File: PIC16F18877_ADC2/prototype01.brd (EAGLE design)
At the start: 72 x 47 mm, 18 parts, among them CN1 PIC_CN_H, CN2 12V_IN, CN3 ADC_IN, SW1 10-XX, U1 XC6202P502TB, U2 PIC16F18877-I/P, X1 20MHz

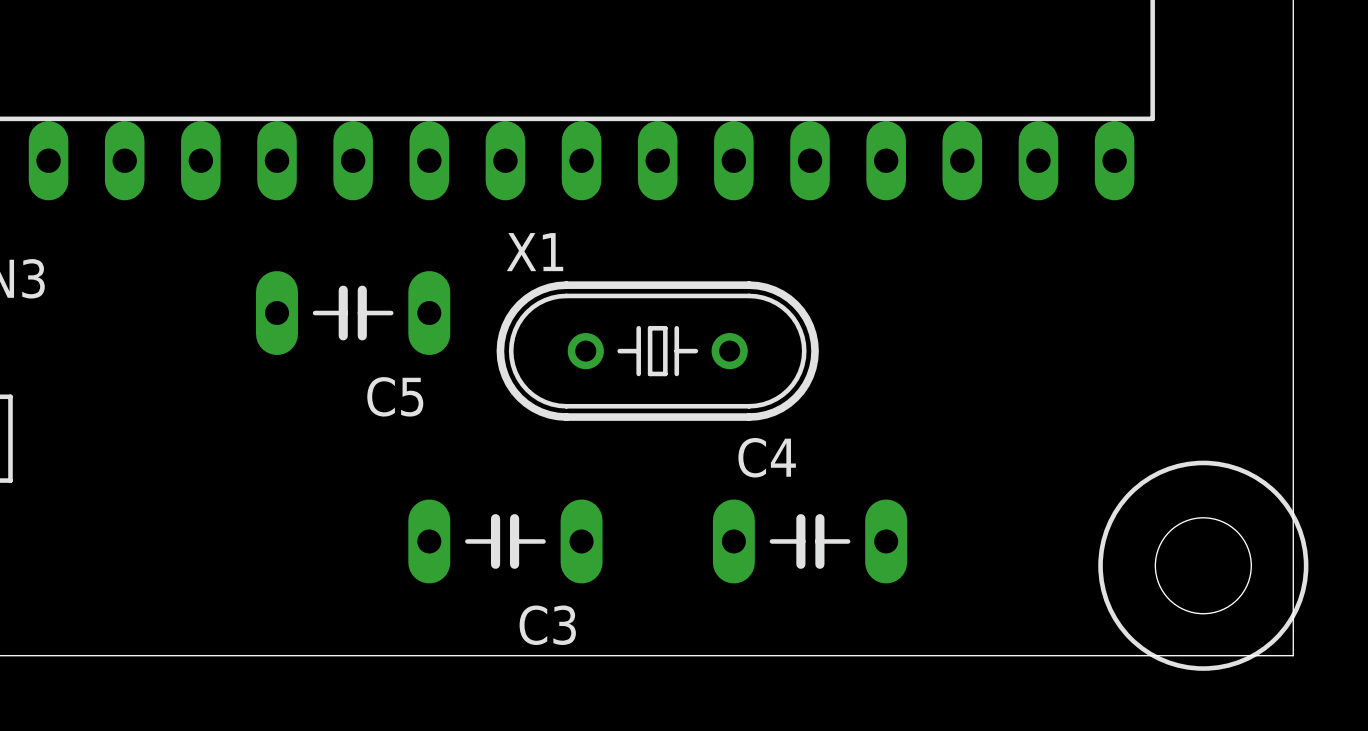
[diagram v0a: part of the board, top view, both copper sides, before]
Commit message: 回路図を修正
LCDモジュール(AE-AQM1602A)を回路に追加
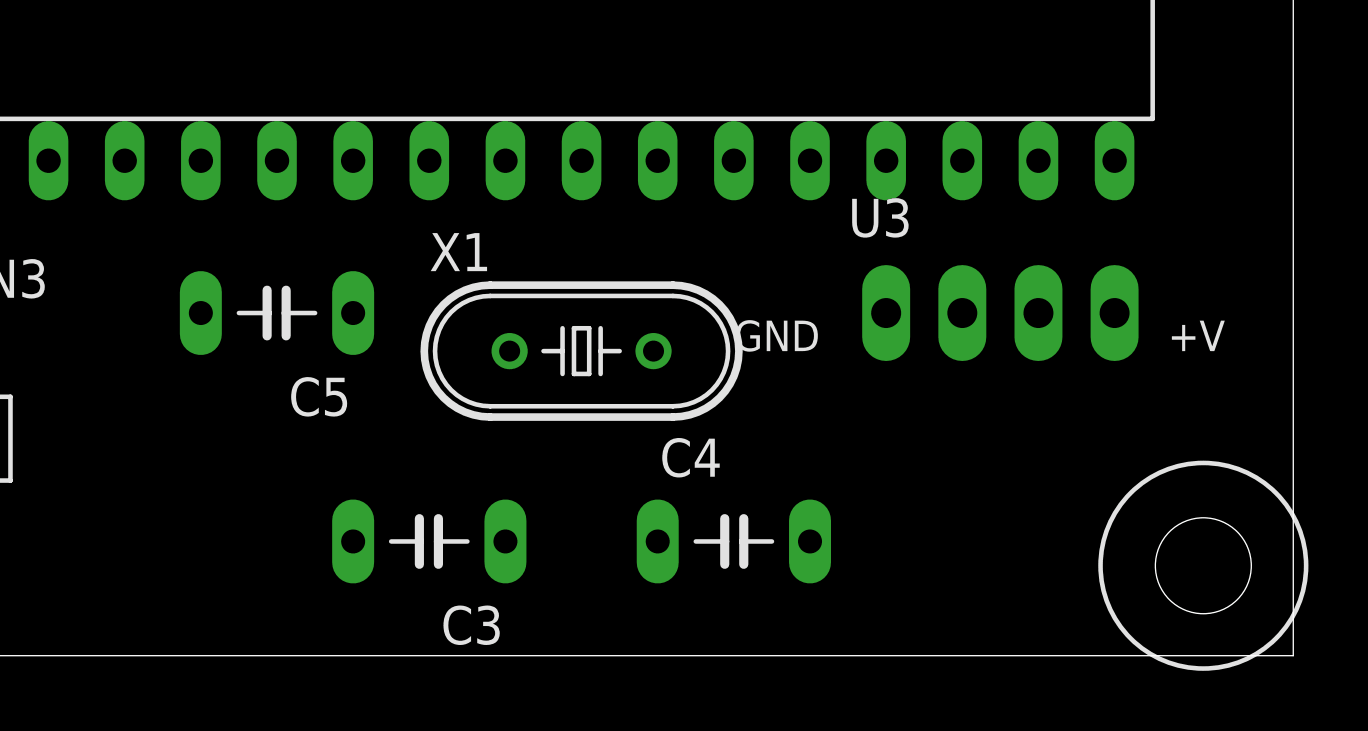
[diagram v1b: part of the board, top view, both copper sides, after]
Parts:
- added U3: AE-AQM1602A, PartsForProto:AE-AQM1602A
- moved C3 2.54 mm to (43.2, 3.81)
- moved C4 2.54 mm to (53.3, 3.81)
- moved C5 2.54 mm to (38.1, 11.4)
- moved X1 2.54 mm to (48.3, 10.2)
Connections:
- new net N$1: U2.18, U3.3
- new net N$5: U2.23, U3.2
- net +5V: now also U3.4
- net 0V: now also U3.1
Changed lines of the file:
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@@
 <element name="C1" library="Parts" package="CAP_200MIL" value="1uF" x="13.97" y="38.1" rot="R270"/>
 <element name="C2" library="Parts" package="CAP_200MIL" value="1uF" x="26.67" y="38.1" rot="R270"/>
-<element name="C3" library="Parts" package="CAP_200MIL" value="22pF" x="45.72" y="3.81" rot="R180"/>
-<element name="C4" library="Parts" package="CAP_200MIL" value="22pF" x="55.88" y="3.81"/>
-<element name="C5" library="Parts" package="CAP_200MIL" value="0.1uF" x="40.64" y="11.43" rot="R180"/>
+<element name="C3" library="Parts" package="CAP_200MIL" value="22pF" x="43.18" y="3.81" rot="R180"/>
+<element name="C4" library="Parts" package="CAP_200MIL" value="22pF" x="53.34" y="3.81"/>
+<element name="C5" library="Parts" package="CAP_200MIL" value="0.1uF" x="38.1" y="11.43" rot="R180"/>
 <element name="C6" library="Parts" package="CAP_200MIL" value="0.1uF" x="35.56" y="36.83" rot="R180"/>
 <element name="CN1" library="Connectors" package="HEADER_6PIN" value="PIC_CN_H" x="7.62" y="25.4" rot="R90"/>
@@
 <element name="U1" library="Parts" package="TO92-LINE" value="XC6202P502TB" x="17.78" y="40.64"/>
 <element name="U2" library="Parts" package="DIL40" value="PIC16F18877-I/P" x="41.91" y="24.13"/>
-<element name="X1" library="Parts" package="HC-49/S" value="20MHz" x="50.8" y="10.16"/>
+<element name="X1" library="Parts" package="HC-49/S" value="20MHz" x="48.26" y="10.16"/>
 <element name="H1" library="Generic" package="3,2" value="MOUNT_HOLE_3.2" x="3" y="44"/>
 <element name="H2" library="Generic" package="3,2" value="MOUNT_HOLE_3.2" x="3" y="3"/>
@@
 <element name="H4" library="Generic" package="3,2" value="MOUNT_HOLE_3.2" x="69" y="44"/>
 <element name="CN2" library="Connectors" package="HEADER_L_2PIN" value="12V_IN" x="19.05" y="8.89" rot="R180"/>
+<element name="U3" library="PartsForProto" package="AE-AQM1602A" value="AE-AQM1602A" x="58.42" y="11.43"/>
 </elements>
 <signals>
@@
 <contactref element="CN3" pad="2"/>
 <contactref element="CN2" pad="2"/>
-<wire x1="40.64" y1="31.75" x2="33.02" y2="36.83" width="0" layer="19" extent="1-1"/>
+<contactref element="U3" pad="1"/>
+<wire x1="33.02" y1="36.83" x2="40.64" y2="31.75" width="0" layer="19" extent="1-1"/>
 <wire x1="26.67" y1="35.56" x2="33.02" y2="36.83" width="0" layer="19" extent="1-1"/>
 <wire x1="20.32" y1="40.64" x2="26.67" y2="35.56" width="0" layer="19" extent="1-1"/>
@@
 <wire x1="3.81" y1="15.24" x2="7.62" y2="30.48" width="0" layer="19" extent="1-1"/>
 <wire x1="3.81" y1="10.16" x2="3.81" y2="15.24" width="0" layer="19" extent="1-1"/>
-<wire x1="20.32" y1="10.16" x2="3.81" y2="10.16" width="0" layer="19" extent="1-1"/>
 <wire x1="45.72" y1="16.51" x2="40.64" y2="31.75" width="0" layer="19" extent="1-1"/>
-<wire x1="38.1" y1="11.43" x2="45.72" y2="16.51" width="0" layer="19" extent="1-1"/>
-<wire x1="58.42" y1="3.81" x2="38.1" y2="11.43" width="0" layer="19" extent="1-1"/>
-<wire x1="43.18" y1="3.81" x2="38.1" y2="11.43" width="0" layer="19" extent="1-1"/>
-<wire x1="27.94" y1="10.16" x2="3.81" y2="10.16" width="0" layer="19" extent="1-1"/>
+<wire x1="35.56" y1="11.43" x2="45.72" y2="16.51" width="0" layer="19" extent="1-1"/>
+<wire x1="40.64" y1="3.81" x2="35.56" y2="11.43" width="0" layer="19" extent="1-1"/>
+<wire x1="27.94" y1="10.16" x2="35.56" y2="11.43" width="0" layer="19" extent="1-1"/>
+<wire x1="20.32" y1="10.16" x2="27.94" y2="10.16" width="0" layer="19" extent="1-1"/>
+<wire x1="55.88" y1="3.81" x2="40.64" y2="3.81" width="0" layer="19" extent="1-1"/>
+<wire x1="58.42" y1="11.43" x2="3.81" y2="10.16" width="0" layer="19" extent="1-1"/>
 </signal>
 <signal name="+5V">
@@
 <contactref element="U2" pad="32"/>
 <contactref element="CN1" pad="2"/>
-<wire x1="7.62" y1="27.94" x2="11.43" y2="20.32" width="0" layer="19" extent="1-1"/>
-<wire x1="43.18" y1="11.43" x2="7.62" y2="27.94" width="0" layer="19" extent="1-1"/>
-<wire x1="38.1" y1="36.83" x2="43.18" y2="11.43" width="0" layer="19" extent="1-1"/>
+<contactref element="U3" pad="4"/>
+<wire x1="38.1" y1="31.75" x2="38.1" y2="36.83" width="0" layer="19" extent="1-1"/>
+<wire x1="43.18" y1="16.51" x2="38.1" y2="31.75" width="0" layer="19" extent="1-1"/>
+<wire x1="40.64" y1="11.43" x2="43.18" y2="16.51" width="0" layer="19" extent="1-1"/>
 <wire x1="17.78" y1="40.64" x2="38.1" y2="36.83" width="0" layer="19" extent="1-1"/>
 <wire x1="13.97" y1="40.64" x2="17.78" y2="40.64" width="0" layer="19" extent="1-1"/>
-<wire x1="38.1" y1="31.75" x2="17.78" y2="40.64" width="0" layer="19" extent="1-1"/>
-<wire x1="43.18" y1="16.51" x2="38.1" y2="31.75" width="0" layer="19" extent="1-1"/>
+<wire x1="7.62" y1="27.94" x2="13.97" y2="40.64" width="0" layer="19" extent="1-1"/>
+<wire x1="11.43" y1="20.32" x2="7.62" y2="27.94" width="0" layer="19" extent="1-1"/>
+<wire x1="66.04" y1="11.43" x2="11.43" y2="20.32" width="0" layer="19" extent="1-1"/>
 </signal>
 <signal name="OSC1">
@@
 <contactref element="C3" pad="1"/>
 <contactref element="U2" pad="13"/>
-<wire x1="48.4" y1="10.16" x2="48.26" y2="16.51" width="0" layer="19" extent="1-1"/>
-<wire x1="48.26" y1="3.81" x2="48.4" y2="10.16" width="0" layer="19" extent="1-1"/>
+<wire x1="45.86" y1="10.16" x2="48.26" y2="16.51" width="0" layer="19" extent="1-1"/>
+<wire x1="45.72" y1="3.81" x2="45.86" y2="10.16" width="0" layer="19" extent="1-1"/>
 </signal>
 <signal name="OSC2">
@@
 <contactref element="C4" pad="1"/>
 <contactref element="U2" pad="14"/>
-<wire x1="53.2" y1="10.16" x2="50.8" y2="16.51" width="0" layer="19" extent="1-1"/>
-<wire x1="53.34" y1="3.81" x2="53.2" y2="10.16" width="0" layer="19" extent="1-1"/>
+<wire x1="50.66" y1="10.16" x2="50.8" y2="16.51" width="0" layer="19" extent="1-1"/>
+<wire x1="50.8" y1="3.81" x2="50.66" y2="10.16" width="0" layer="19" extent="1-1"/>
 </signal>
 <signal name="N$3">
@@
 <wire x1="25.4" y1="10.16" x2="20.32" y2="16.51" width="0" layer="19" extent="1-1"/>
 </signal>
+<signal name="N$1">
+<contactref element="U3" pad="3"/>
+<contactref element="U2" pad="18"/>
+<wire x1="63.5" y1="11.43" x2="60.96" y2="16.51" width="0" layer="19" extent="1-1"/>
+</signal>
+<signal name="N$5">
+<contactref element="U3" pad="2"/>
+<contactref element="U2" pad="23"/>
+<wire x1="60.96" y1="11.43" x2="60.96" y2="31.75" width="0" layer="19" extent="1-1"/>
+</signal>
 </signals>

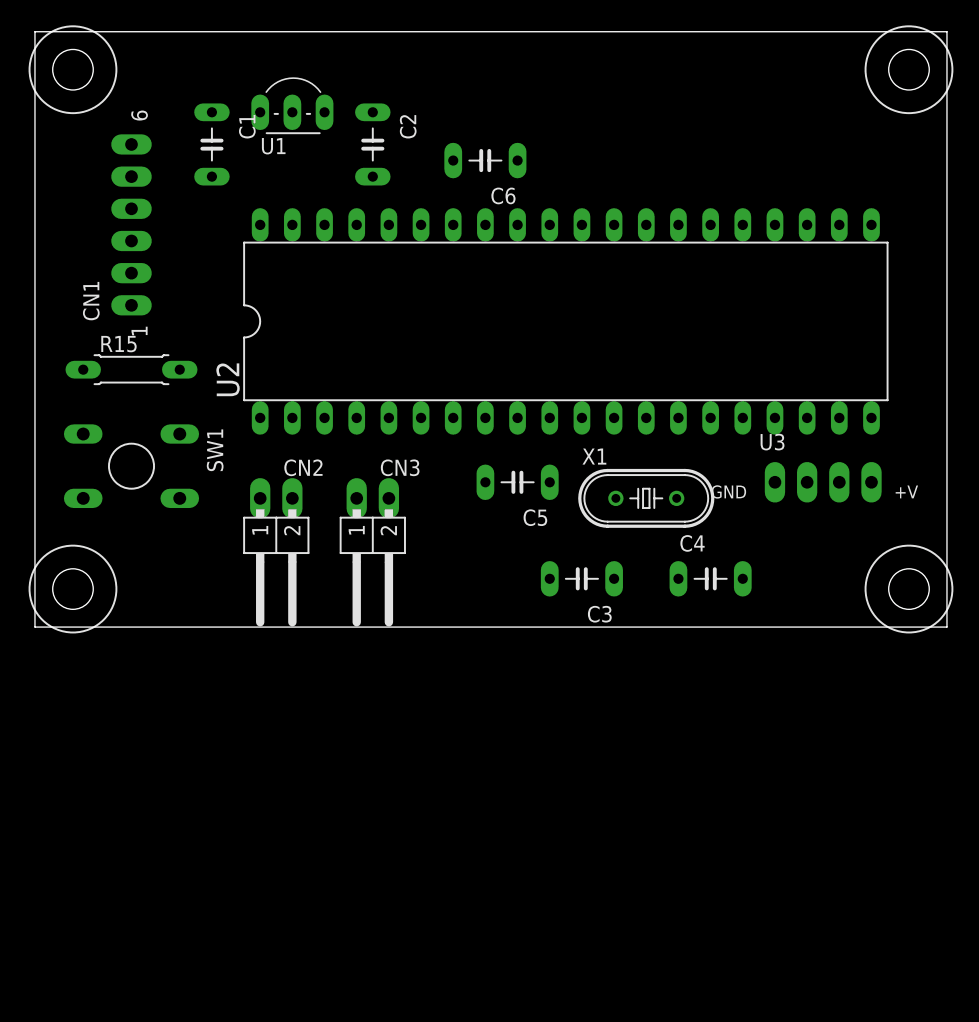
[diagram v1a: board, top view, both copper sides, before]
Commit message: I2C LCD開通時の回路図
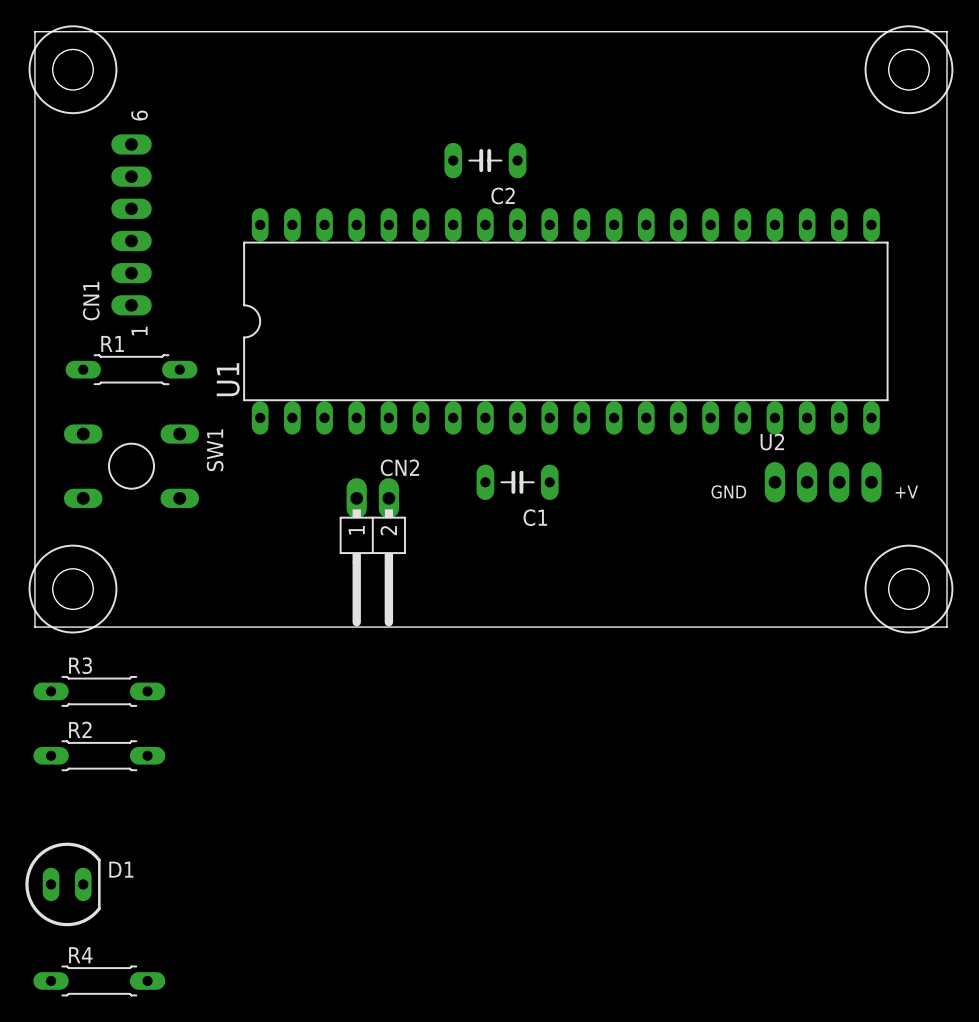
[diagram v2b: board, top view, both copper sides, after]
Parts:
- removed C3, C4: 22pF, Parts:CAP_200MIL
- removed C5, C6: 0.1uF, Parts:CAP_200MIL
- removed CN3: ADC_IN, Connectors:HEADER_L_2PIN
- removed U3: AE-AQM1602A, PartsForProto:AE-AQM1602A
- removed X1: 20MHz, Parts:HC-49/S
- added D1: LED_5MM, Parts:LED5MM
- added R2, R3, R4: 10k, Parts:RESISTOR_0207_300MIL
- C1, C2: value 1uF -> 0.1uF
- CN2: value 12V_IN -> ADC_IN
- U1: value XC6202P502TB -> PIC16F18877-I/P; device Parts:TO92-LINE -> Parts:DIL40
- U2: value PIC16F18877-I/P -> AE-AQM1602A; device Parts:DIL40 -> PartsForProto:AE-AQM1602A
- moved C1 36.0 mm to (38.1, 11.4), turned to 180 degrees
- moved U1 29.2 mm to (41.9, 24.1)
- moved U2 20.8 mm to (58.4, 11.4)
- moved C2 8.98 mm to (35.6, 36.8), turned to 180 degrees
- moved CN2 7.62 mm to (26.7, 8.89)
- renumbered R15 to R1
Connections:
- removed net +12V: C2.1, CN2.1, U1.3
- removed net N$5: U2.23, U3.2
- removed net OSC1: C3.1, U2.13, X1.1
- removed net OSC2: C4.1, U2.14, X1.2
- new net HCK_LED: D1.A, U1.3
- new net SCL1: R2.1, U1.18, U2.3
- new net SDA1: R3.1, U1.23, U2.2
- net +5V: now also C2.1, R2.2, R3.2, U1.11, U1.32, U2.4; no longer C5.1, C6.1, U1.1, U2.11, U2.32, U3.4
- net 0V: now also R4.1, U1.12, U1.31, U2.1; no longer C3.2, C4.2, C5.2, C6.2, CN3.2, U1.2, U2.12, U2.31, U3.1
- net ANA0: now also CN2.1, U1.2; no longer CN3.1, U2.2
- net N$1: now also D1.K, R4.2; no longer U2.18, U3.3
- net N$2: now also U1.40; no longer U2.40
- net N$3: now also U1.1; no longer U2.1
- net N$4: now also U1.39; no longer U2.39

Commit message: 配線を修正
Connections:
- net HCK_LED: now also U1.21; no longer U1.3
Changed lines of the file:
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@@
 </signal>
 <signal name="HCK_LED">
-<contactref element="U1" pad="3"/>
 <contactref element="D1" pad="A"/>
-<wire x1="1.27" y1="-20.32" x2="22.86" y2="16.51" width="0" layer="19" extent="1-1"/>
+<contactref element="U1" pad="21"/>
+<wire x1="1.27" y1="-20.32" x2="66.04" y2="31.75" width="0" layer="19" extent="1-1"/>
 </signal>
 <signal name="N$1">
